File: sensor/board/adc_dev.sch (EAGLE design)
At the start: 6 parts, among them U1 FT232RL-BASICSSOP

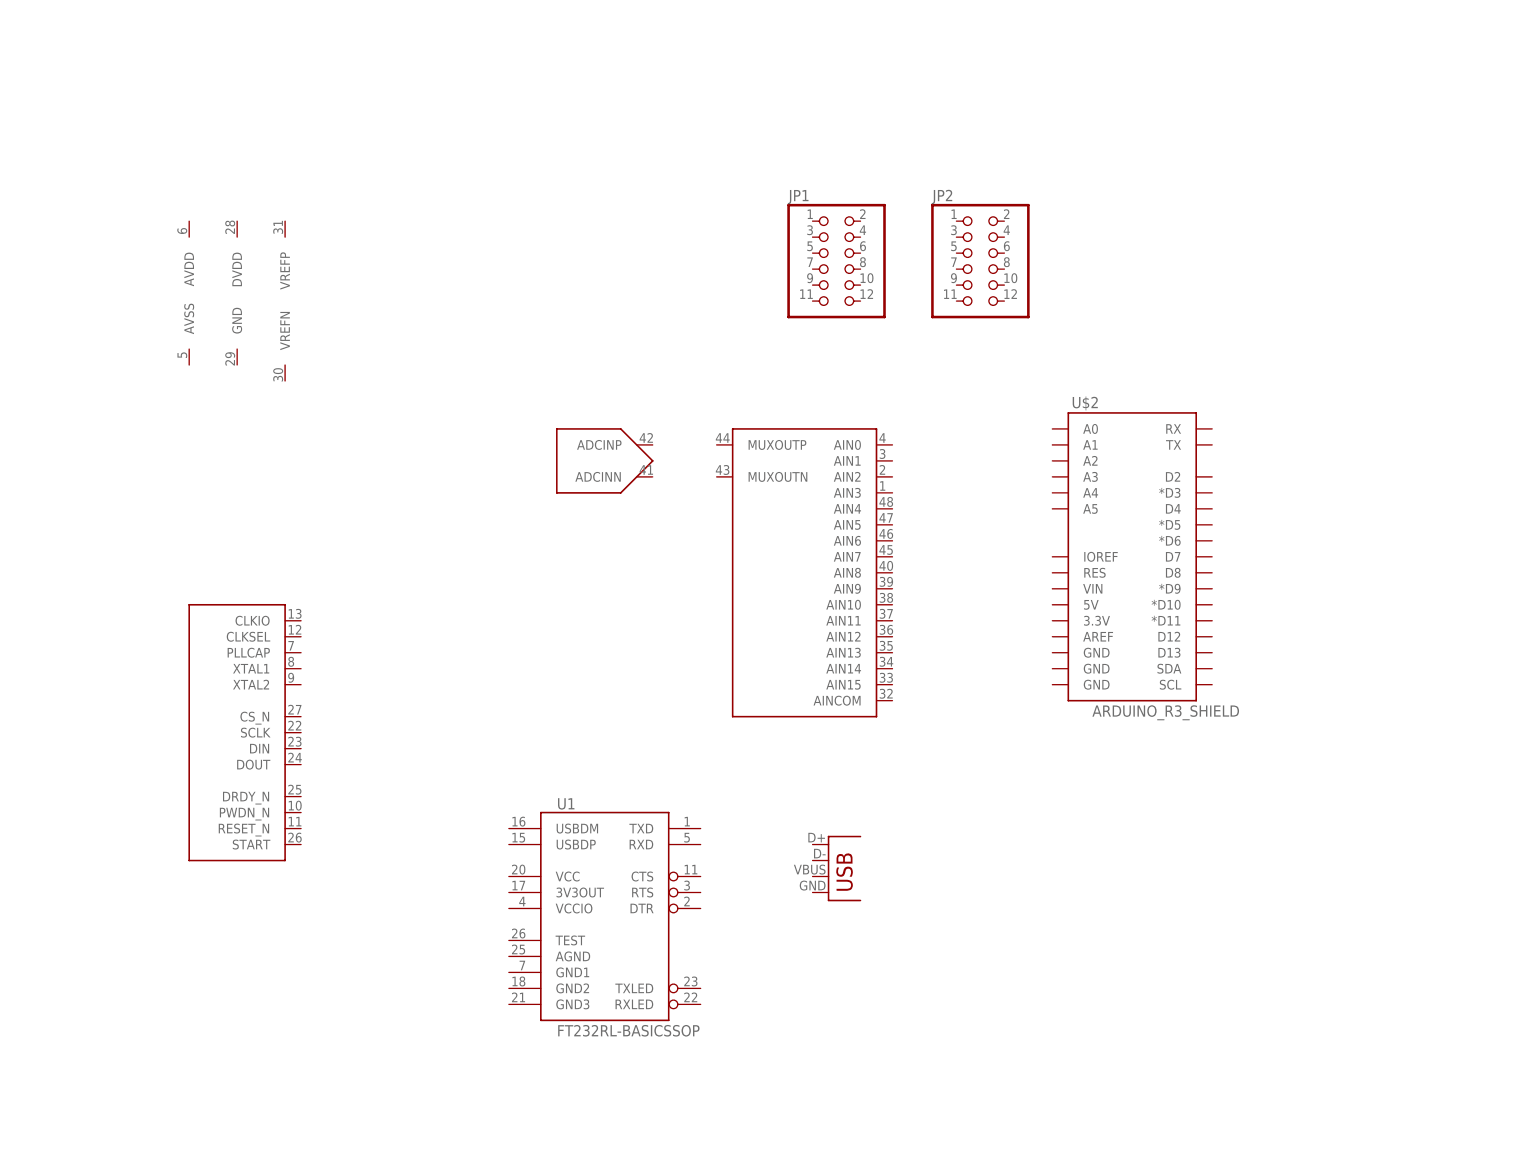
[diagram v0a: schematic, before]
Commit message: Schematic pretty much done, need to pinswap before layout
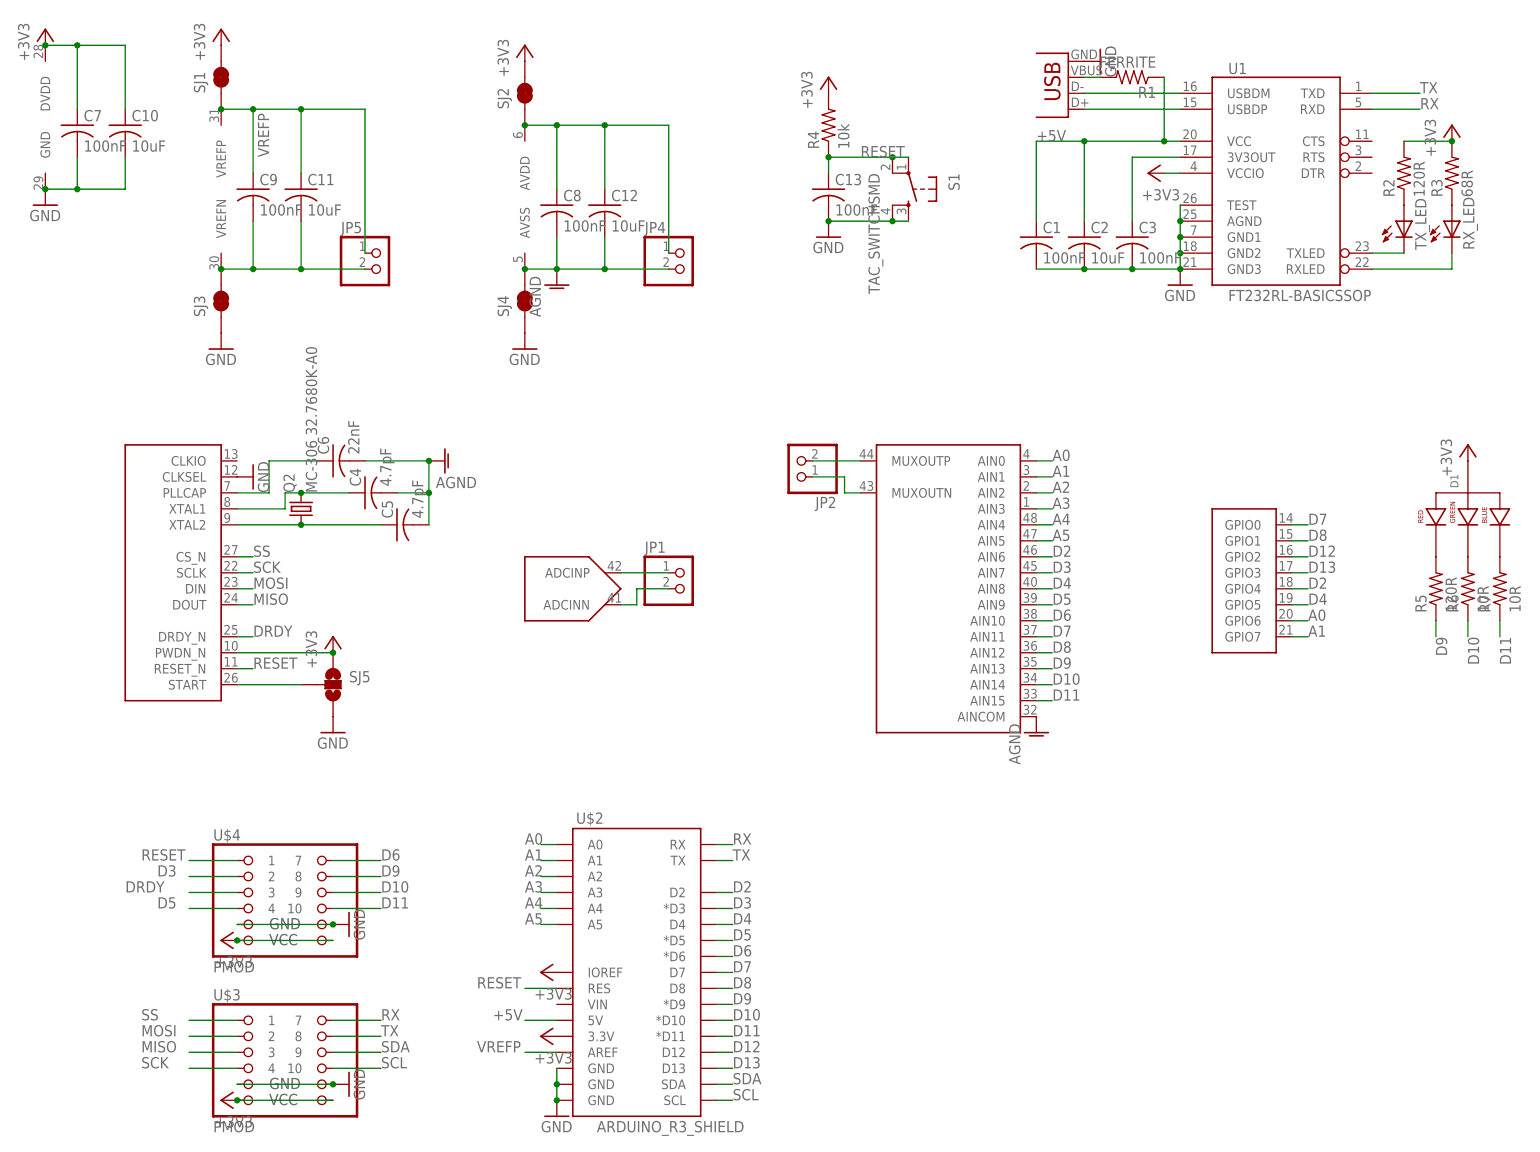
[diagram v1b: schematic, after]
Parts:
- added C1, C13, C3, C7, C8, C9: 100nF, rcl:C-USC0603
- added C10, C11, C12, C2: 10uF, rcl:C-USC0603
- added C4, C5: 4.7pF, rcl:C-USC0603
- added C6: 22nF, rcl:C-USC0603
- added D1: LED-RGB-CA-THRUCLEAR, SparkFun-LED:LED-RGB-CA-THRUCLEAR
- added JP4, JP5: (no value), pinhead:PINHD-1X2
- added Q2: MC-306 32.7680K-A0, crystal:MC-306
- added R1: FERRITE, rcl:R-US_R0603
- added R2, R5: 120R, rcl:R-US_R0603
- added R3: 68R, rcl:R-US_R0603
- added R4: 10k, rcl:R-US_R0603
- added R6, R7: 10R, rcl:R-US_R0603
- added RX_LED, TX_LED: (no value), led:LEDCHIPLED_0603
- added S1: TAC_SWITCHSMD, SparkFun-Electromechanical:TAC_SWITCHSMD
- added SJ1, SJ2, SJ3, SJ4: JUMPER-PAD-2-NC_BY_TRACE, SparkFun-Passives:JUMPER-PAD-2-NC_BY_TRACE
- added SJ5: JUMPER-PAD-3-NOFULL_BOX_SILK, SparkFun-Passives:JUMPER-PAD-3-NOFULL_BOX_SILK
- added U$3, U$4: PMOD, modular_robotics:PMOD
- JP1, JP2: device pinhead:PINHD-2X6 -> pinhead:PINHD-1X2
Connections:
- new net +3V3: C10.1, C7.1, D1.ANODE, R2.2, R3.2, R4.2, SJ1.2, SJ2.2, SJ5.1, U$1CTRL.PWDN_N, U$1GND-DVDD.DVDD, U$2.3.3V, U$2.IOREF, U$3.12, U$3.6, U$4.12, U$4.6, U1.VCCIO
- new net +5V: C1.1, C2.1, R1.1, U$2.5V, U1.VCC
- new net A0: U$1GPIO.GPIO6, U$1MUX.AIN0, U$2.A0
- new net A1: U$1GPIO.GPIO7, U$1MUX.AIN1, U$2.A1
- new net A2: U$1MUX.AIN2, U$2.A2
- new net A3: U$1MUX.AIN3, U$2.A3
- new net A4: U$1MUX.AIN4, U$2.A4
- new net A5: U$1MUX.AIN5, U$2.A5
- new net AGND: C12.2, C4.2, C5.2, C6.2, C8.2, JP4.2, SJ4.2, U$1AVDD-AVSS.AVSS, U$1MUX.AINCOM
- new net D10: R6.1, U$1MUX.AIN14, U$2.*D10, U$4.9
- new net D11: R7.1, U$1MUX.AIN15, U$2.*D11, U$4.10
- new net D12: U$1GPIO.GPIO2, U$2.D12
- new net D13: U$1GPIO.GPIO3, U$2.D13
- new net D2: U$1GPIO.GPIO4, U$1MUX.AIN6, U$2.D2
- new net D3: U$1MUX.AIN7, U$2.*D3, U$4.2
- new net D4: U$1GPIO.GPIO5, U$1MUX.AIN8, U$2.D4
- new net D5: U$1MUX.AIN9, U$2.*D5, U$4.4
- new net D6: U$1MUX.AIN10, U$2.*D6, U$4.7
- new net D7: U$1GPIO.GPIO0, U$1MUX.AIN11, U$2.D7
- new net D8: U$1GPIO.GPIO1, U$1MUX.AIN12, U$2.D8
- new net D9: R5.1, U$1MUX.AIN13, U$2.*D9, U$4.8
- new net DRDY: U$1CTRL.DRDY_N, U$4.3
- new net GND: C1.2, C10.2, C13.2, C2.2, C3.2, C7.2, JP3.GND, S1.3, S1.4, SJ3.1, SJ4.1, SJ5.3, U$1CTRL.CLKSEL, U$1GND-DVDD.GND, U$2.GND@0, U$2.GND@1, U$2.GND@2, U$3.11, U$3.5, U$4.11, U$4.5, U1.AGND, U1.GND1, U1.GND2, U1.GND3, U1.TEST
- new net MISO: U$1CTRL.DOUT, U$3.3
- new net MOSI: U$1CTRL.DIN, U$3.2
- new net N$1: JP3.D+, U1.USBDP
- new net N$10: JP1.1, U$1ADC.ADCINP
- new net N$11: C12.1, C8.1, JP4.1, SJ2.1, U$1AVDD-AVSS.AVDD
- new net N$12: C11.2, C9.2, JP5.2, SJ3.2, U$1VREFN-VREFP.VREFN
- new net N$13: C6.1, U$1CTRL.PLLCAP
- new net N$14: C4.1, Q2.2, U$1CTRL.XTAL1
- new net N$15: C5.1, Q2.1, U$1CTRL.XTAL2
- new net N$16: JP1.2, U$1ADC.ADCINN
- new net N$17: D1.RED_CATHODE, R5.2
- new net N$18: D1.GREEN_CATHODE, R6.2
- new net N$19: JP2.2, U$1MUX.MUXOUTP
- new net N$2: JP3.D-, U1.USBDM
- new net N$20: JP2.1, U$1MUX.MUXOUTN
- new net N$21: D1.BLUE_CATHODE, R7.2
- new net N$3: R2.1, TX_LED.A
- new net N$4: R3.1, RX_LED.A
- new net N$5: C3.1, U1.3V3OUT
- new net N$6: SJ5.2, U$1CTRL.START
- new net N$7: JP3.VBUS, R1.2
- new net N$8: TX_LED.C, U1.TXLED
- new net N$9: RX_LED.C, U1.RXLED
- new net RESET: C13.1, R4.1, S1.1, S1.2, U$1CTRL.RESET_N, U$2.RES, U$4.1
- new net RX: U$2.RX, U$3.7, U1.RXD
- new net SCK: U$1CTRL.SCLK, U$3.4
- new net SCL: U$2.SCL, U$3.10
- new net SDA: U$2.SDA, U$3.9
- new net SS: U$1CTRL.CS_N, U$3.1
- new net TX: U$2.TX, U$3.8, U1.TXD
- new net VREFP: C11.1, C9.1, JP5.1, SJ1.1, U$1VREFN-VREFP.VREFP, U$2.AREF
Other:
- moved on the sheet: U$2, U1

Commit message: Rough layout getting there
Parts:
- added R8, R9: 4k7, rcl:R-US_R0603
- SJ5: value JUMPER-PAD-3-NOFULL_BOX_SILK -> JUMPER-PAD-3-NOYES_SILK; device SparkFun-Passives:JUMPER-PAD-3-NOFULL_BOX_SILK -> SparkFun-Passives:JUMPER-PAD-3-NOYES_SILK
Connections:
- net +3V3: now also R8.2, R9.2
- net A0: now also U$1GPIO.GPIO1, U$1MUX.AIN5; no longer U$1GPIO.GPIO6, U$1MUX.AIN0
- net A1: now also U$1GPIO.GPIO0, U$1MUX.AIN4; no longer U$1GPIO.GPIO7, U$1MUX.AIN1
- net A2: now also U$1MUX.AIN3; no longer U$1MUX.AIN2
- net A3: now also U$1MUX.AIN2; no longer U$1MUX.AIN3
- net A4: now also U$1MUX.AIN1; no longer U$1MUX.AIN4
- net A5: now also U$1MUX.AIN0; no longer U$1MUX.AIN5
- net AGND: now also U$1EPAD.1
- net D10: now also U$4.8; no longer U$4.9
- net D11: now also U$4.7; no longer U$4.10
- net D12: now also U$1GPIO.GPIO7; no longer U$1GPIO.GPIO2
- net D13: now also U$1GPIO.GPIO5; no longer U$1GPIO.GPIO3
- net D2: now also U$1GPIO.GPIO2; no longer U$1GPIO.GPIO4
- net D3: now also U$1MUX.AIN11, U$4.4; no longer U$1MUX.AIN7, U$4.2
- net D4: now also U$1GPIO.GPIO3, U$1MUX.AIN7; no longer U$1GPIO.GPIO5, U$1MUX.AIN8
- net D5: now also U$1MUX.AIN12, U$4.10; no longer U$1MUX.AIN9, U$4.4
- net D6: now also U$4.2; no longer U$4.7
- net D7: now also U$1GPIO.GPIO4, U$1MUX.AIN8; no longer U$1GPIO.GPIO0, U$1MUX.AIN11
- net D8: now also U$1GPIO.GPIO6, U$1MUX.AIN9; no longer U$1GPIO.GPIO1, U$1MUX.AIN12
- net D9: now also U$4.9; no longer U$4.8
- net MISO: now also U$3.9; no longer U$3.3
- net MOSI: now also U$3.8; no longer U$3.2
- net N$14: now also Q2.1; no longer Q2.2
- net N$15: now also Q2.2; no longer Q2.1
- net RX: now also U$3.1; no longer U$3.7
- net SCK: now also U$3.7; no longer U$3.4
- net SCL: now also R9.1, U$3.4; no longer U$3.10
- net SDA: now also R8.1, U$3.3; no longer U$3.9
- net SS: now also U$3.10; no longer U$3.1
- net TX: now also U$3.2; no longer U$3.8
